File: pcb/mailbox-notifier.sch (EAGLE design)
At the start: 70 parts, among them CON1 3P-SH-SIDE, Q1 AO3401, U1 MCP73832, U10 MIC2019, U11 74LVC1G17, U2 MIC23155, U3 FS312F-G, U4 FS8205, U5 EFM32PG1B200F256GM32, U6 SST26VF016B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

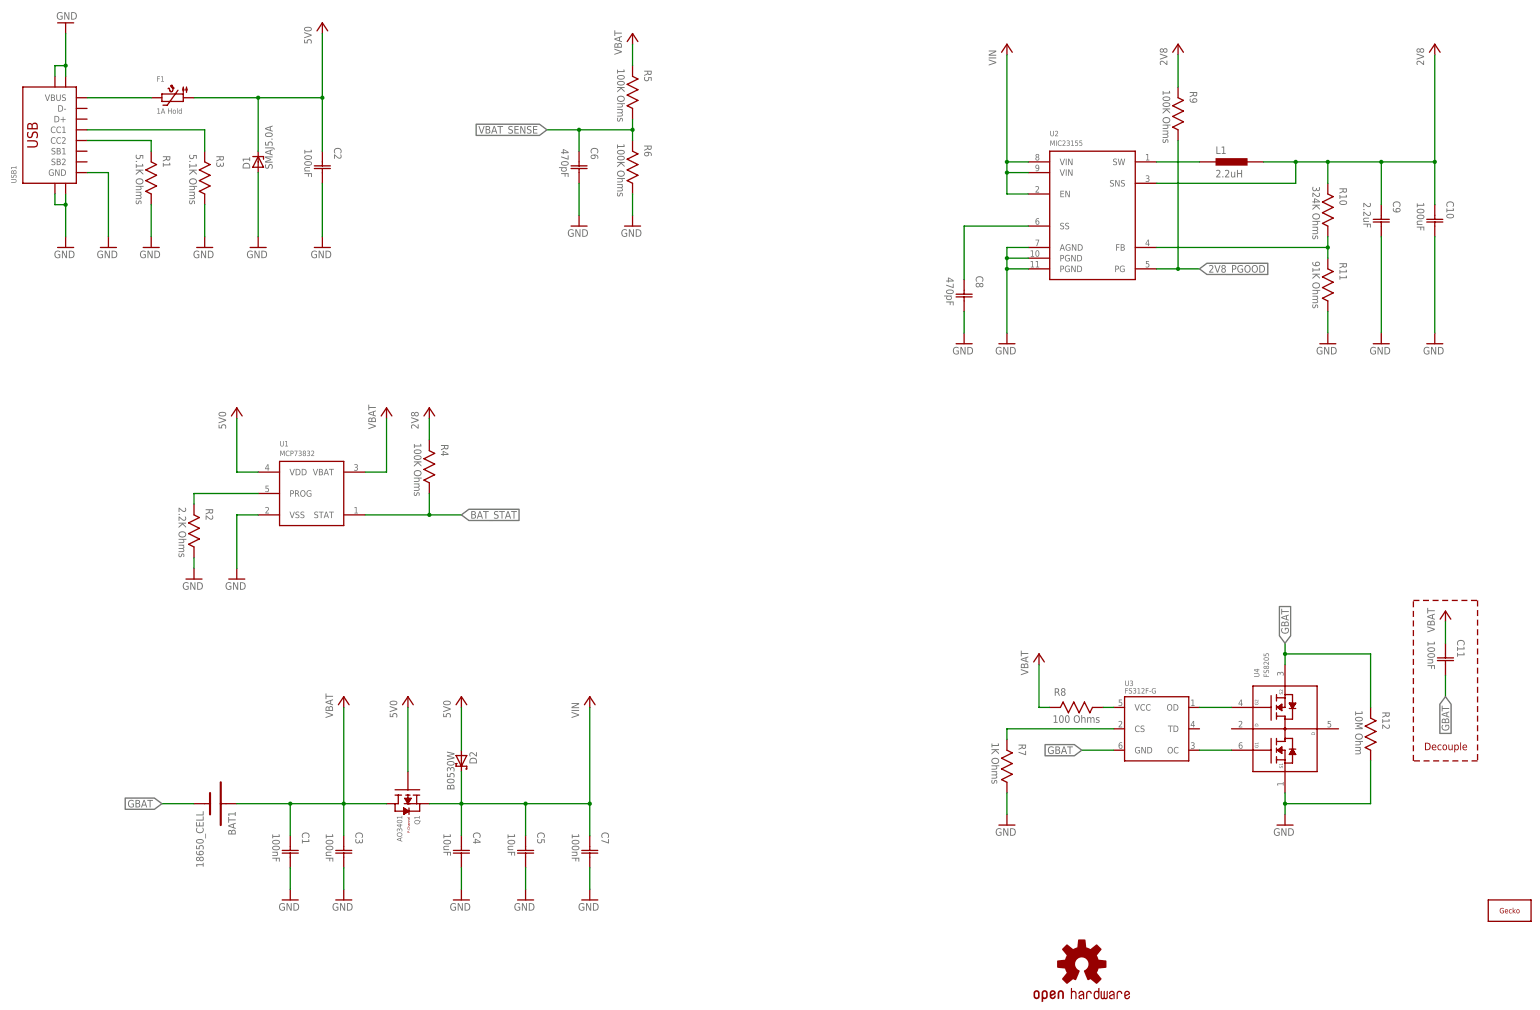
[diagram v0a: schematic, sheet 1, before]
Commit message: Sync library updates Add schematic PDF
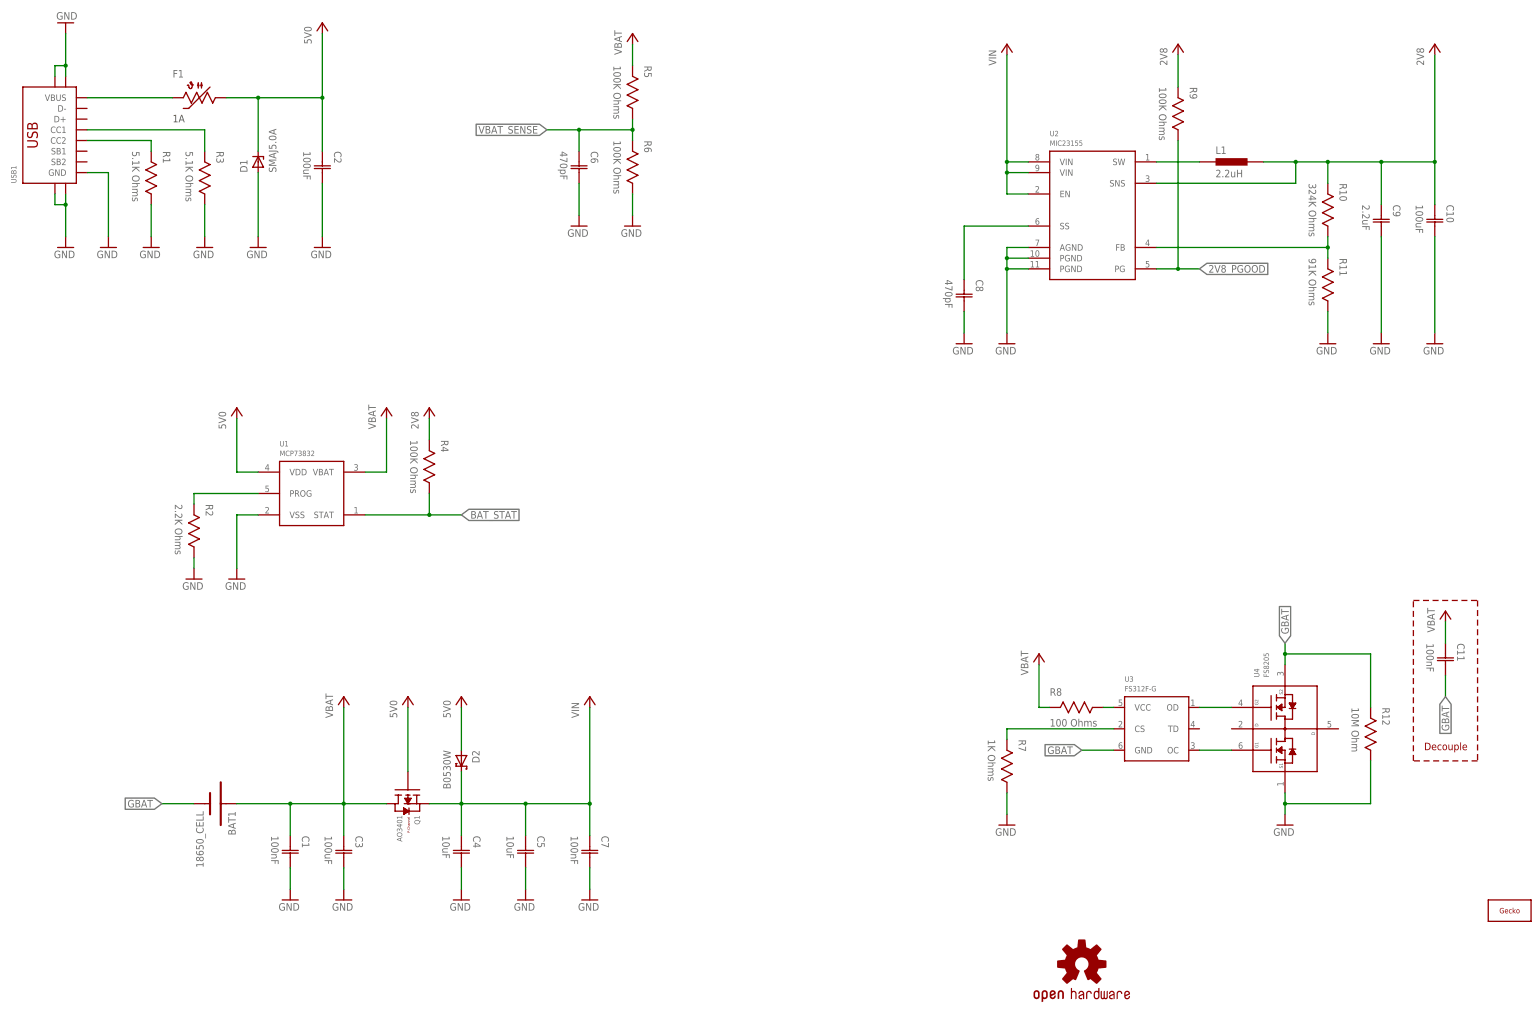
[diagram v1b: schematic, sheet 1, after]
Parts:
- F1: HOLD (none) -> 1A
